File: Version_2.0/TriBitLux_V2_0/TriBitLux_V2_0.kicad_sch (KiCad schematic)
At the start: 38 parts, among them J2 Conn_01x02_Pin, U1 LM339, U2 LM339, U3 74LS148, U4 74LS48, U5 D198K

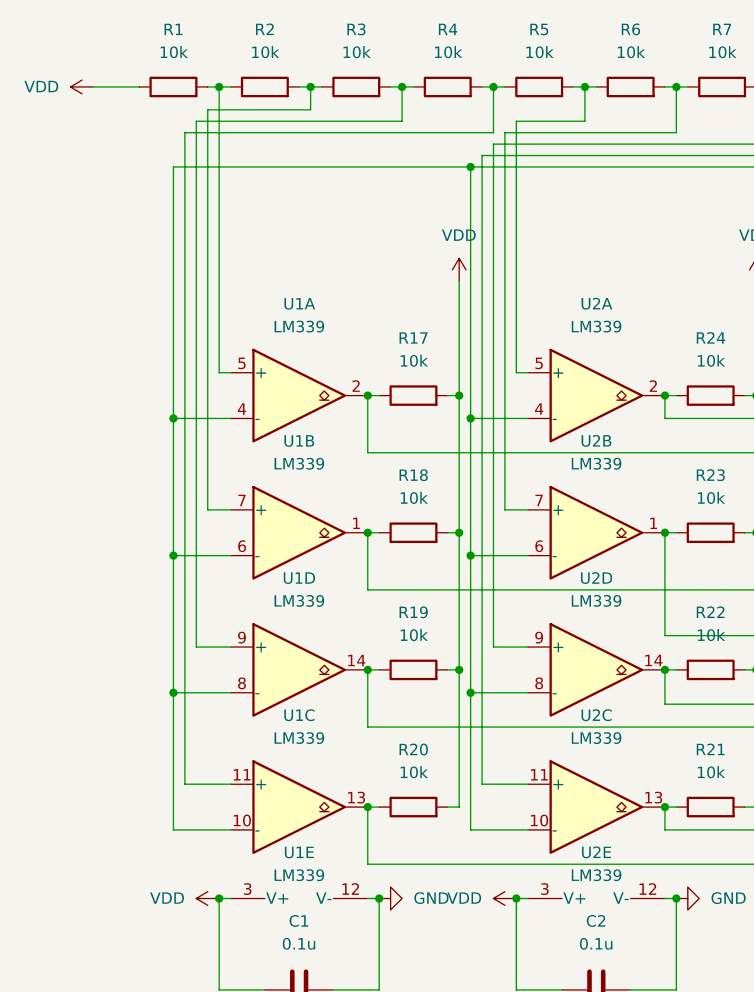
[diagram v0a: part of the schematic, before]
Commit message: Input of the Comparator is reversed to make it work with active low priority encoder. The output of the comparator is now connected to the active low input of the priority encoder.
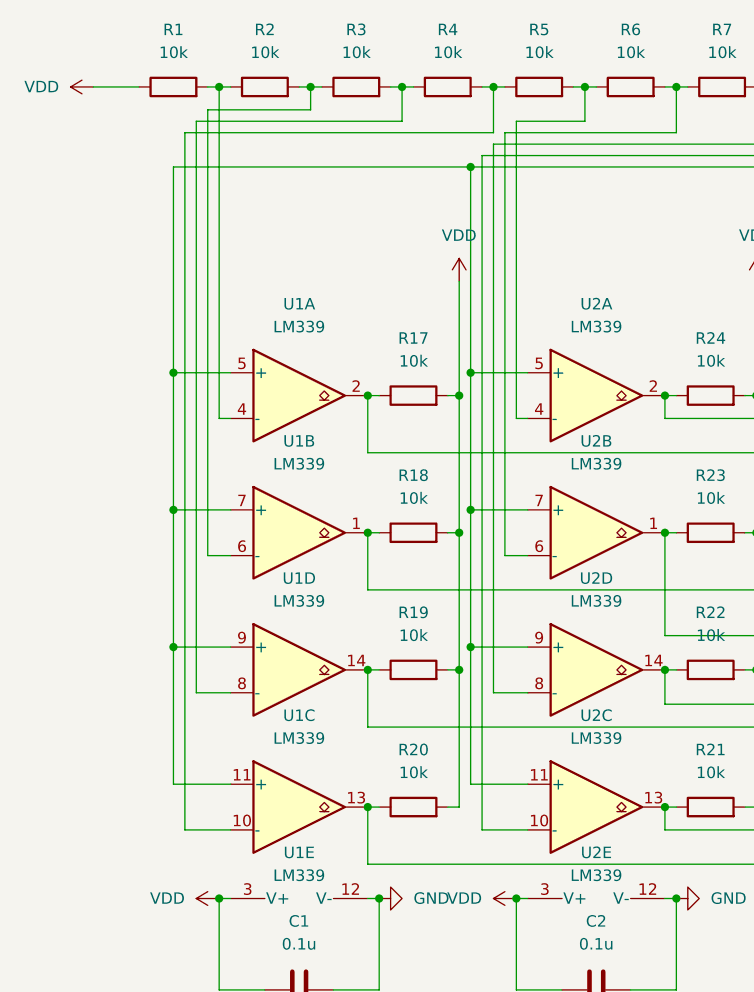
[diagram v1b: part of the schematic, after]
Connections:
- net GND: now also U2.10 (-); no longer U2.11 (+)
- net at R5.2, R6.1: now also U2.4 (-); no longer U2.5 (+)
- net at R6.2, R7.1: now also U2.6 (-); no longer U2.7 (+)
- net at R1.2, R2.1: now also U1.4 (-); no longer U1.5 (+)
- net at R2.2, R3.1: now also U1.6 (-); no longer U1.7 (+)
- net at R7.2, R8.1: now also U2.8 (-); no longer U2.9 (+)
- net at R3.2, R4.1: now also U1.8 (-); no longer U1.9 (+)
- net at R4.2, R5.1: now also U1.10 (-); no longer U1.11 (+)
- new net: R9.1, RV1.1, U1.11 (+), U1.5 (+), U1.7 (+), U1.9 (+), U2.11 (+), U2.5 (+), U2.7 (+), U2.9 (+)

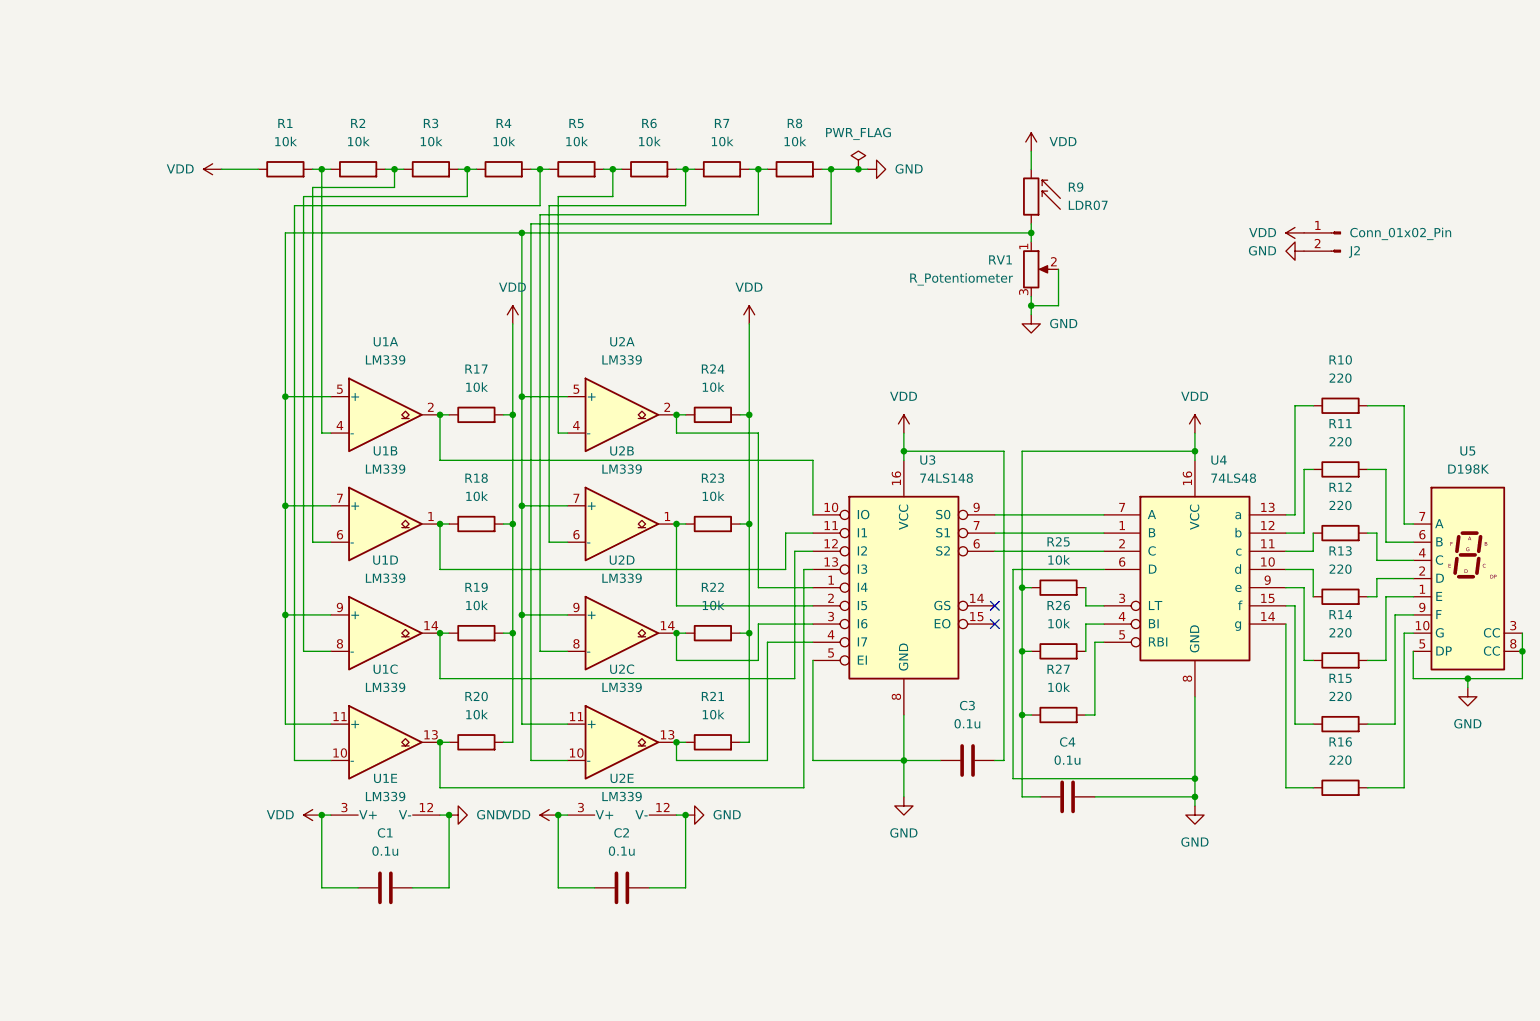
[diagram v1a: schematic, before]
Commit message: Schematics Fix and Update: As the circuit was only counting from 1 to 7 and debugged it to count from 0 to 7, Reference voltage of LDR and Resistor was changed to 3.3V from 5V.
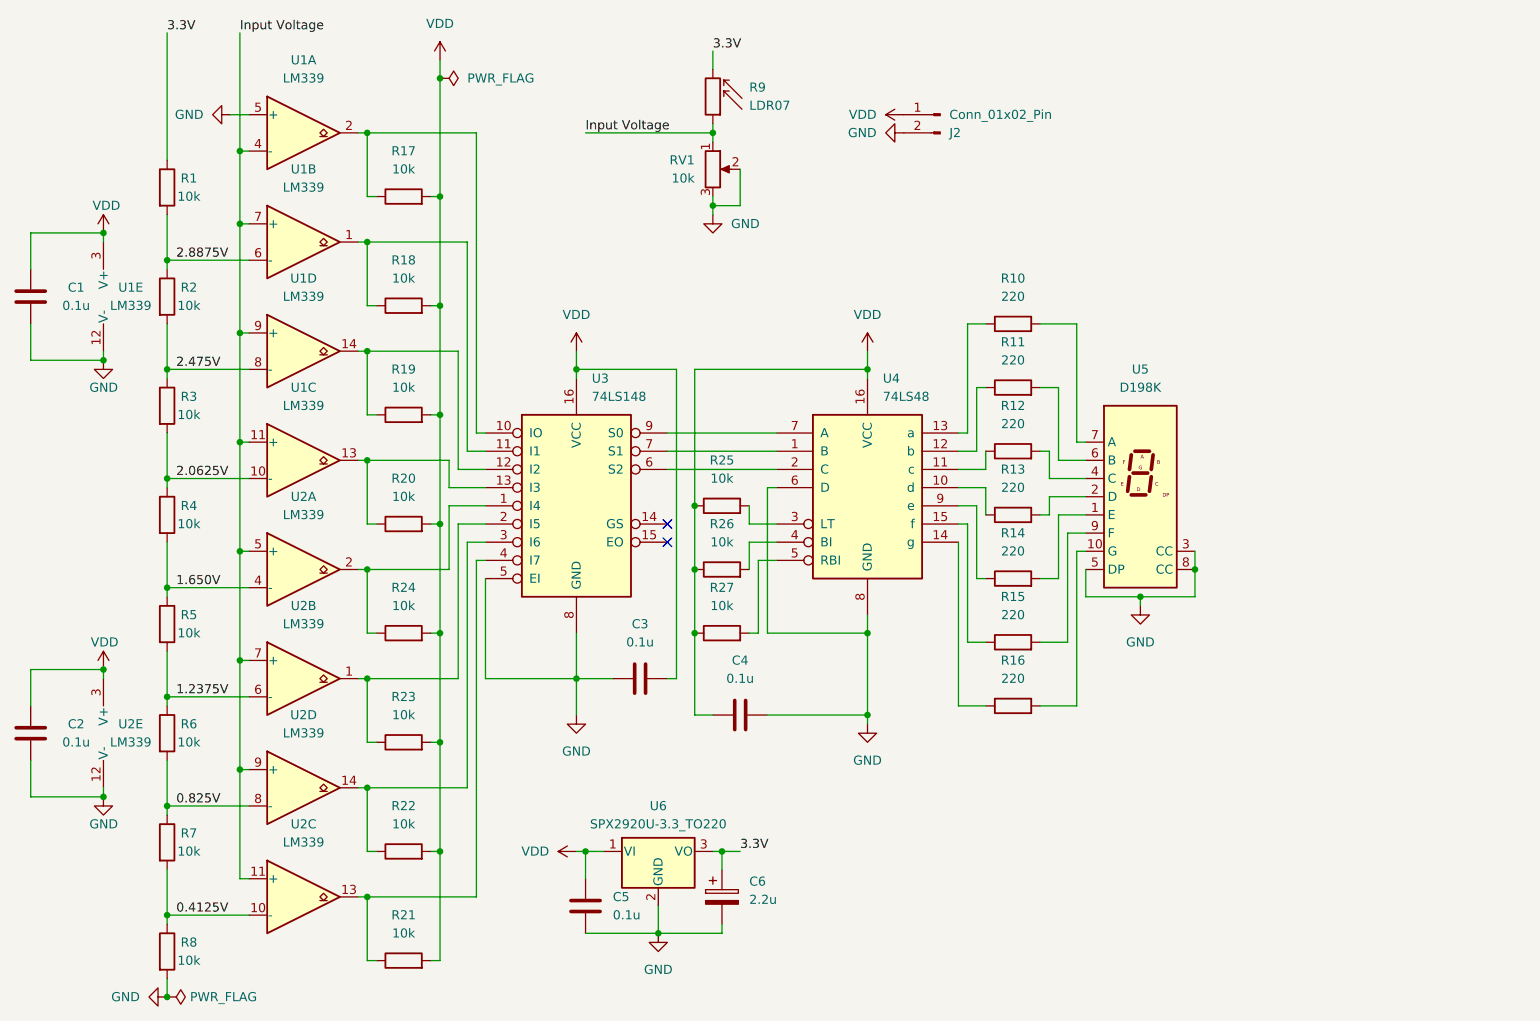
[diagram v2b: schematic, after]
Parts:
- added C5: 0.1u, Capacitor_THT:C_Disc_D5.0mm_W2.5mm_P5.00mm, symbol Device:C
- added C6: 2.2u, Capacitor_THT:CP_Radial_D5.0mm_P2.00mm, symbol Device:C_Polarized
- added U6: SPX2920U-3.3_TO220, Package_TO_SOT_THT:TO-220-3_Vertical, symbol Regulator_Linear:SPX2920U-3.3_TO220
- RV1: value R_Potentiometer -> 10k
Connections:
- net GND: now also U1.5 (+), C5.2, C6.2, U6.2 (GND); no longer U2.10 (-)
- net VDD: now also C5.1, U6.1 (VI); no longer R1.1, R9.2
- net 1.2375V: now reaches R5.2, R6.1
- net 1.2375V: now also U2.6 (-); no longer U2.4 (-)
- net 0.825V: now reaches R6.2, R7.1
- net 0.825V: now also U2.8 (-); no longer U2.6 (-)
- net 2.8875V: now reaches R1.2, R2.1
- net 2.8875V: now also U1.6 (-); no longer U1.4 (-)
- net 2.475V: now reaches R2.2, R3.1
- net 2.475V: now also U1.8 (-); no longer U1.6 (-)
- net 0.4125V: now reaches R7.2, R8.1
- net 0.4125V: now also U2.10 (-); no longer U2.8 (-)
- net 2.0625V: now reaches R3.2, R4.1
- net 2.0625V: now also U1.10 (-); no longer U1.8 (-)
- net Input Voltage: now reaches R9.1, RV1.1, U1.11 (+), U1.7 (+), U1.9 (+), U2.11 (+), U2.5 (+), U2.7 (+), U2.9 (+)
- net Input Voltage: now also U1.4 (-); no longer U1.5 (+)
- net 1.650V: now reaches R4.2, R5.1
- net 1.650V: now also U2.4 (-); no longer U1.10 (-)
- new net 3.3V: C6.1, R1.1, R9.2, U6.3 (VO)
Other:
- moved on the sheet: C1, C2, C3, C4, J2, R1, R10, R11, R12, R13, R14, R15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

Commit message: 3V3 Design Update
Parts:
- C1, C2, C3, C4: footprint Capacitor_THT:C_Disc_D10.0mm_W2.5mm_P5.00mm -> Extra Footprints:C_Disc_D5.0mm_W2.5mm_P5.00mm_ClearSilk
- C5: footprint Capacitor_THT:C_Disc_D5.0mm_W2.5mm_P5.00mm -> Extra Footprints:C_Disc_D5.0mm_W2.5mm_P5.00mm_ClearSilk
- C6: footprint Capacitor_THT:CP_Radial_D5.0mm_P2.00mm -> Extra Footprints:CP_Radial_D5.0mm_P2.00mm_ClearSilk
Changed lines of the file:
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@@
 			)
 		)
-		(property "Footprint" "Capacitor_THT:C_Disc_D10.0mm_W2.5mm_P5.00mm"
+		(property "Footprint" "Extra Footprints:C_Disc_D5.0mm_W2.5mm_P5.00mm_ClearSilk"
 			(at 113.03 129.2352 0)
 			(effects
@@
 			)
 		)
-		(property "Footprint" "Capacitor_THT:CP_Radial_D5.0mm_P2.00mm"
+		(property "Footprint" "Extra Footprints:CP_Radial_D5.0mm_P2.00mm_ClearSilk"
 			(at 129.2352 162.56 0)
 			(effects
@@
 			)
 		)
-		(property "Footprint" "Capacitor_THT:C_Disc_D10.0mm_W2.5mm_P5.00mm"
+		(property "Footprint" "Extra Footprints:C_Disc_D5.0mm_W2.5mm_P5.00mm_ClearSilk"
 			(at 32.7152 78.74 0)
 			(effects
@@
 			)
 		)
-		(property "Footprint" "Capacitor_THT:C_Disc_D10.0mm_W2.5mm_P5.00mm"
+		(property "Footprint" "Extra Footprints:C_Disc_D5.0mm_W2.5mm_P5.00mm_ClearSilk"
 			(at 127 134.3152 0)
 			(effects
@@
 			)
 		)
-		(property "Footprint" "Capacitor_THT:C_Disc_D5.0mm_W2.5mm_P5.00mm"
+		(property "Footprint" "Extra Footprints:C_Disc_D5.0mm_W2.5mm_P5.00mm_ClearSilk"
 			(at 110.1852 163.83 0)
 			(effects
@@
 			)
 		)
-		(property "Footprint" "Capacitor_THT:C_Disc_D10.0mm_W2.5mm_P5.00mm"
+		(property "Footprint" "Extra Footprints:C_Disc_D5.0mm_W2.5mm_P5.00mm_ClearSilk"
 			(at 32.7152 139.7 0)
 			(effects
